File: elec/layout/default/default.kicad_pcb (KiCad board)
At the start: 4 copper layers, 76 x 146 mm, 103 parts, among them J1 ?, J2 ?, Q1 ?, SW1 ?, SW10 ?, SW11 ?, SW12 ?, SW13 ?, SW14 ?, SW15 ?, SW16 ?, SW17 ?, SW18 ?, SW19 ?, SW2 ?, SW20 ?, SW21 ?, SW22 ?, SW23 ?, SW24 ?, SW25 ?, SW26 ?, SW27 ?, SW28 ?, SW29 ?, SW3 ?, SW30 ?, SW31 ?, SW32 ?, SW33 ?, SW34 ?, SW35 ?, SW36 ?, SW37 ?, SW38 ?, SW39 ?, SW4 ?, SW40 ?, SW5 ?, SW6 ?, SW7 ?, SW8 ?, SW9 ?, U1 ?, U2 ?, U3 ?, U4 ?, U5 ?, U6 ?, U7 ?, U8 ?

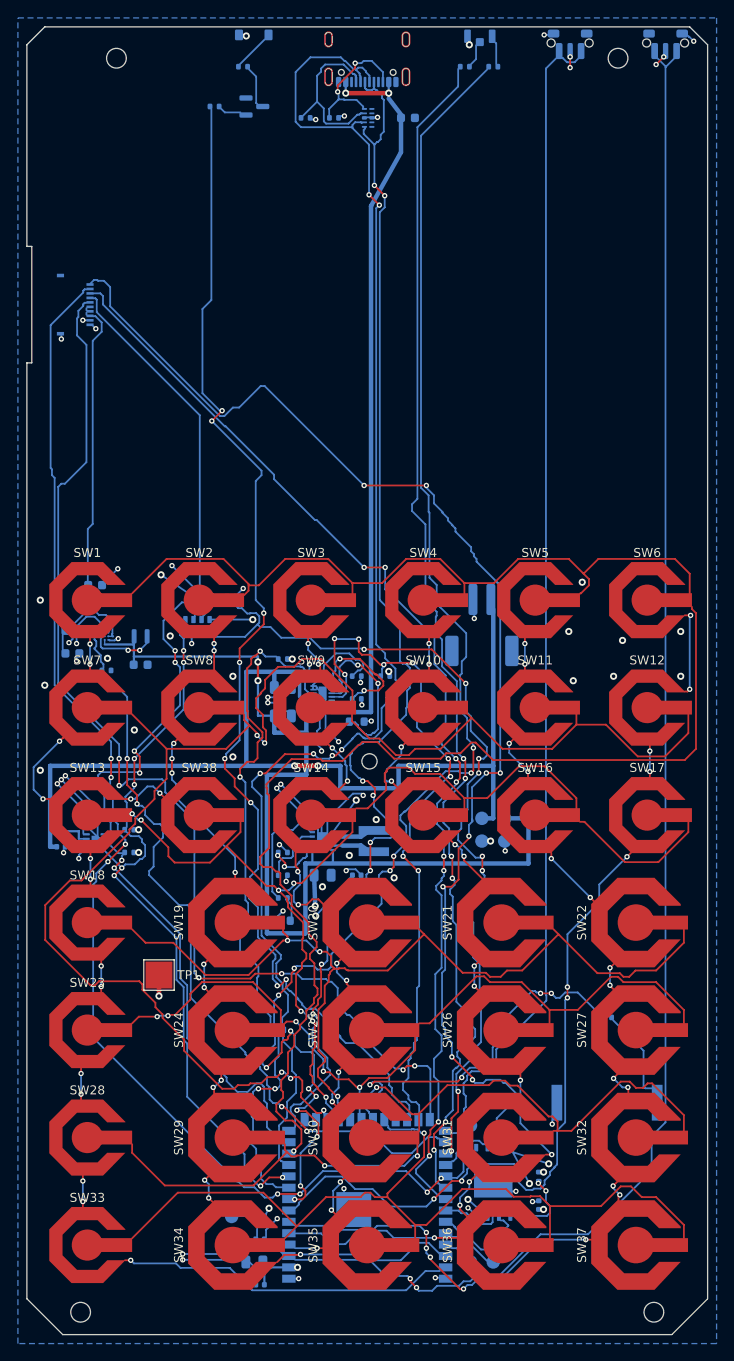
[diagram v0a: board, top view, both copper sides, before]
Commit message: mip: vendor 3D models; RV-8263 and FH34SRJ land fixes; full reroute
Barnaby's vendor STEP for U6 (TPS61099YFFT), U7 (RV-8263-C7), U8 (Micron
MT29F2G01) and J2 (Hirose FH34SRJ-10S) replace the stand-ins. Landing them
caught two footprint faults:

- RV-8263-C7: the land had been copied from the datasheet's bottom view,
  so it was mirrored. Fixed in the generator, library and board (U7).
- FH34SRJ: the catalogue's 3.3 mm is the mounting pattern's overall
  height, not centre to centre, so the fitting lands were 0.8 mm too far
  out (now 2.5). The mouth is 3.025 from the pad row, not 3.70, so J2
  moves to X 6.375 to keep the mouth at X 3.35 and the tail's slack.

The YFF0006 clearance override is now in the generator. route_signals:
a ground-tail via the grid squeezes in with no room to nudge is replaced
by a track to a neighbouring ground pad (U1 pin 3 beside usb_dm).
Stripped and fully rerouted: audit, check_ends, check_pour clean.

Co-Authored-By: Claude Opus 5.5 (1M context) <noreply@anthropic.com>
Claude-Session: https://claude.ai/code/session_01Fsrot3PauY1JdFC7HgzJ33
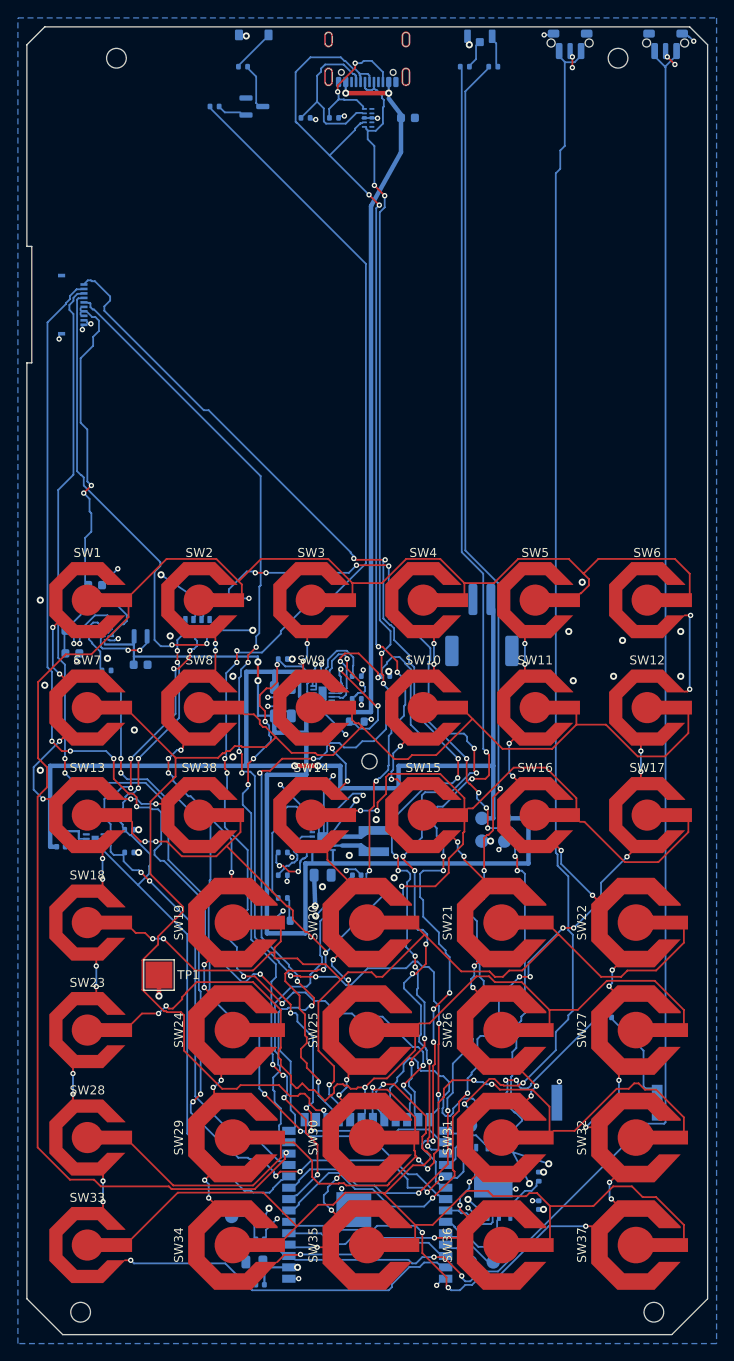
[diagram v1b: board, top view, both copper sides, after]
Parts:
- moved J2 0.67 mm to (6.38, 31.0)
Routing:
- net gnd: track 125.6 -> 74.9 mm, vias 72 -> 62
- net row0: track 200.1 -> 180.1 mm
- net chg_stat2: track 92.8 -> 74.6 mm, vias 10 -> 8
- net row1: track 164.0 -> 146.3 mm, vias 5 -> 1
- net ir_led: track 132.2 -> 149.3 mm
- net row2: track 117.7 -> 133.7 mm, vias 7 -> 8
- net mip_sck: track 145.0 -> 132.8 mm
- net i2c_scl: track 86.2 -> 76.1 mm
- net extcomin: track 41.1 -> 50.2 mm, vias 0 -> 2
- net row6: track 95.3 -> 104.3 mm
- net row5: track 91.4 -> 100.0 mm, vias 3 -> 5
- net mip_clkoe: track 97.7 -> 106.0 mm, vias 8 -> 12
- net usb_dm: track 157.1 -> 149.1 mm
- net col5: track 89.8 -> 82.0 mm, vias 9 -> 11
- net col3: track 56.2 -> 48.8 mm
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
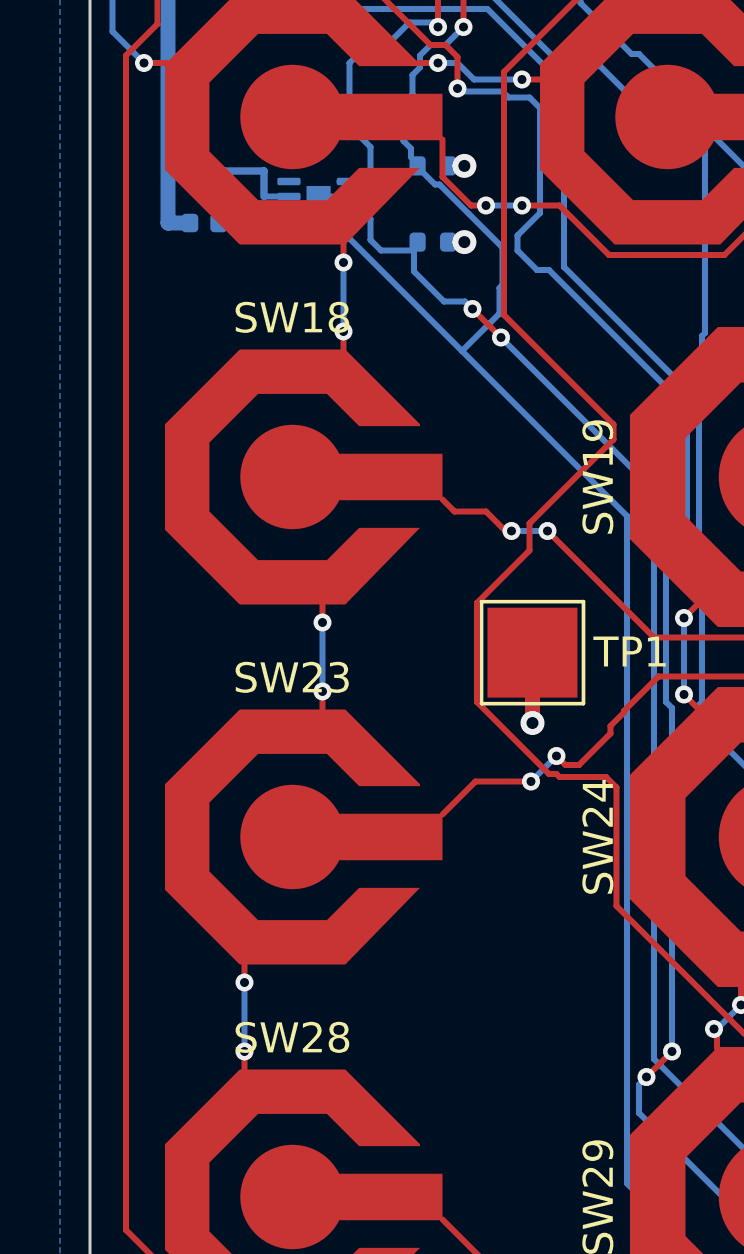
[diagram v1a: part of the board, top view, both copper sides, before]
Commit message: mip: U4 gnd pins 1 and 4 joined to the exposed pad
Barnaby's DRC found U4 pins 1 and 4 unconnected. check_pour counted a pad
as reached when the predicted pour only touched its edge; the pins sit
inside the 0.5 mm clearance of their bat and cell neighbours, so the pour
stopped on their boundary. It now needs real overlap, flags exactly those
two, and route_signals ties each to U4's exposed pad (0.36 mm). check_pour
is now part of route_signals' cache key, since it decides which pads are
stranded. Audit, check_ends, check_pour clean.

Co-Authored-By: Claude Opus 5.5 (1M context) <noreply@anthropic.com>
Claude-Session: https://claude.ai/code/session_01Fsrot3PauY1JdFC7HgzJ33
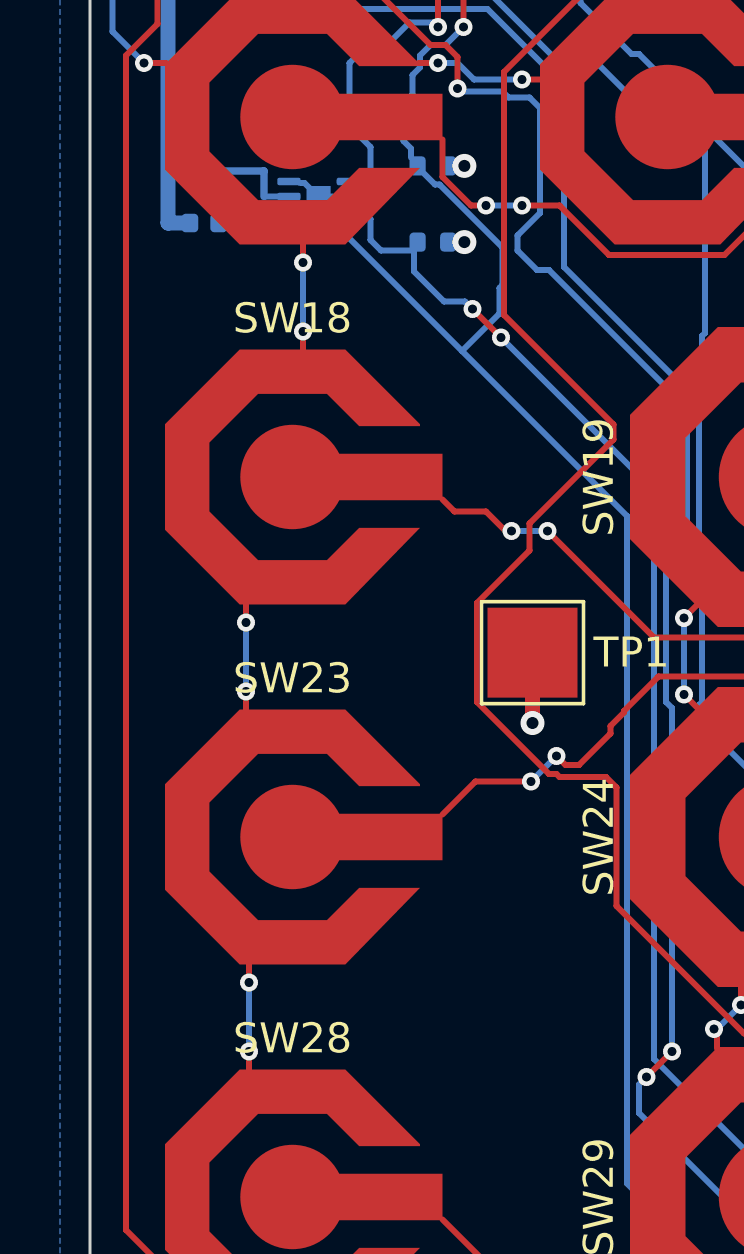
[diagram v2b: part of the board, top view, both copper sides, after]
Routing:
- net gnd: track 74.9 -> 75.6 mm
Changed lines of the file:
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@@
 	)
 	(segment
-		(start 8.45 92.2)
-		(end 8.45 92.85)
+		(start 7.1 92.2)
+		(end 7.1 92.85)
 		(width 0.2)
 		(layer "F.Cu")
@@
 	)
 	(segment
-		(start 8.45 92.85)
-		(end 8.45 95.15)
-		(width 0.2)
-		(layer "B.Cu")
-		(net "col0")
-	)
-	(segment
-		(start 8.45 95.15)
-		(end 8.45 95.8)
+		(start 7.1 92.85)
+		(end 7.1 95.15)
+		(width 0.2)
+		(layer "B.Cu")
+		(net "col0")
+	)
+	(segment
+		(start 7.1 95.15)
+		(end 7.1 95.8)
 		(width 0.2)
 		(layer "F.Cu")
@@
 	)
 	(segment
-		(start 7.75 104.2)
-		(end 7.75 104.85)
+		(start 5.2 104.2)
+		(end 5.2 104.85)
 		(width 0.2)
 		(layer "F.Cu")
@@
 	)
 	(segment
-		(start 7.75 104.85)
-		(end 7.75 107.15)
-		(width 0.2)
-		(layer "B.Cu")
-		(net "col0")
-	)
-	(segment
-		(start 7.75 107.15)
-		(end 7.75 107.8)
+		(start 5.2 104.85)
+		(end 5.2 107.15)
+		(width 0.2)
+		(layer "B.Cu")
+		(net "col0")
+	)
+	(segment
+		(start 5.2 107.15)
+		(end 5.2 107.8)
 		(width 0.2)
 		(layer "F.Cu")
@@
 	)
 	(segment
-		(start 5.15 116.2)
-		(end 5.15 116.85)
+		(start 5.3 116.2)
+		(end 5.3 116.85)
 		(width 0.2)
 		(layer "F.Cu")
@@
 	)
 	(segment
-		(start 5.15 116.85)
-		(end 5.15 119.15)
-		(width 0.2)
-		(layer "B.Cu")
-		(net "col0")
-	)
-	(segment
-		(start 5.15 119.15)
-		(end 5.15 119.8)
+		(start 5.3 116.85)
+		(end 5.3 119.15)
+		(width 0.2)
+		(layer "B.Cu")
+		(net "col0")
+	)
+	(segment
+		(start 5.3 119.15)
+		(end 5.3 119.8)
 		(width 0.2)
 		(layer "F.Cu")
@@
 	)
 	(segment
+		(start 7 91.6)
+		(end 7.15 91.6)
+		(width 0.2)
+		(layer "B.Cu")
+		(net "gnd")
+	)
+	(segment
+		(start 7.15 91.6)
+		(end 7.3 91.45)
+		(width 0.2)
+		(layer "B.Cu")
+		(net "gnd")
+	)
+	(segment
+		(start 7 90.2)
+		(end 7.15 90.2)
+		(width 0.2)
+		(layer "B.Cu")
+		(net "gnd")
+	)
+	(segment
+		(start 7.15 90.2)
+		(end 7.3 90.35)
+		(width 0.2)
+		(layer "B.Cu")
+		(net "gnd")
+	)
+	(segment
 		(start 8.25 90.65)
 		(end 8 90.65)
@@
 	)
 	(via
-		(at 8.45 92.85)
-		(size 0.6)
-		(drill 0.3)
-		(layers "F.Cu" "B.Cu")
-		(net "col0")
-	)
-	(via
-		(at 8.45 95.15)
-		(size 0.6)
-		(drill 0.3)
-		(layers "F.Cu" "B.Cu")
-		(net "col0")
-	)
-	(via
-		(at 7.75 104.85)
-		(size 0.6)
-		(drill 0.3)
-		(layers "F.Cu" "B.Cu")
-		(net "col0")
-	)
-	(via
-		(at 7.75 107.15)
-		(size 0.6)
-		(drill 0.3)
-		(layers "F.Cu" "B.Cu")
-		(net "col0")
-	)
-	(via
-		(at 5.15 116.85)
-		(size 0.6)
-		(drill 0.3)
-		(layers "F.Cu" "B.Cu")
-		(net "col0")
-	)
-	(via
-		(at 5.15 119.15)
-		(size 0.6)
-		(drill 0.3)
+		(at 7.1 92.85)
+		(size 0.6)
+		(drill 0.3)
+		(layers "F.Cu" "B.Cu")
+		(net "col0")
+	)
+	(via
+		(at 7.1 95.15)
+		(size 0.6)
+		(drill 0.3)
+		(layers "F.Cu" "B.Cu")
+		(net "col0")
+	)
+	(via
+		(at 5.2 104.85)
+		(size 0.6)
+		(drill 0.3)
+		(layers "F.Cu" "B.Cu")
+		(net "col0")
+	)
+	(via
+		(at 5.2 107.15)
+		(size 0.6)
+		(drill 0.3)
+		(layers "F.Cu" "B.Cu")
+		(net "col0")
+	)
+	(via
+		(at 5.3 116.85)
+		(size 0.6)
+		(drill 0.3)
+		(layers "F.Cu" "B.Cu")
+		(net "col0")
+	)
+	(via
+		(at 5.3 119.15)
+		(size 0.6)
+		(drill 0.3)

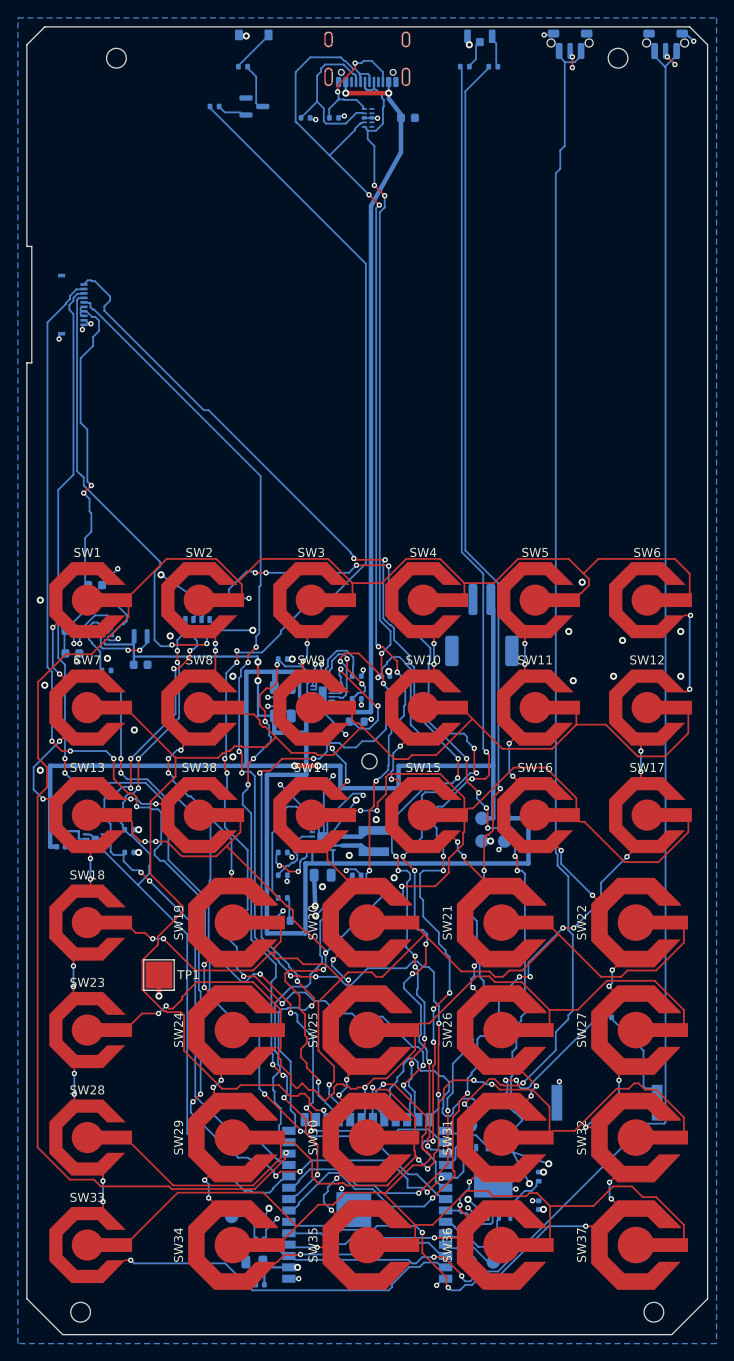
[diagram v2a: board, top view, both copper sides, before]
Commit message: ls027: 2.7in LS027 board placed, IMU+mag, front light switch, power routed
Co-Authored-By: Claude Opus 5.5 (1M context) <noreply@anthropic.com>
Claude-Session: https://claude.ai/code/session_01Fsrot3PauY1JdFC7HgzJ33
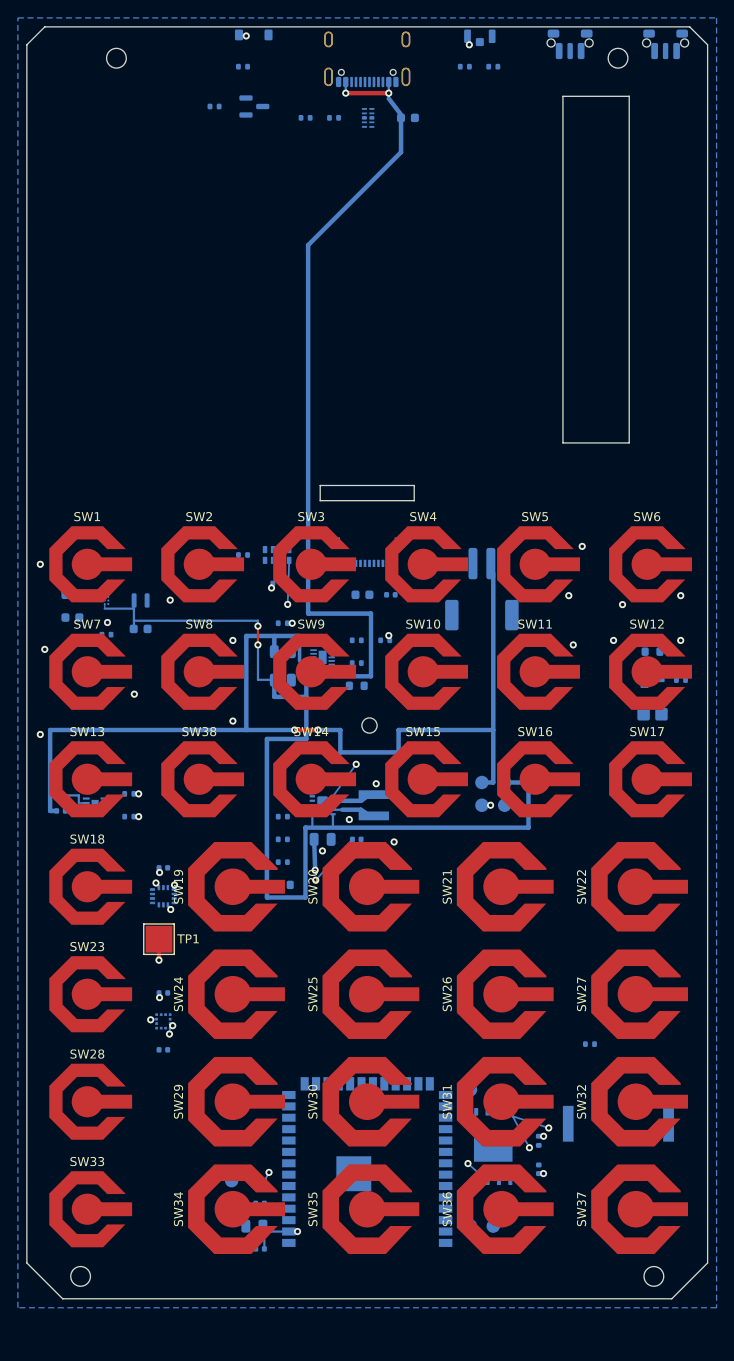
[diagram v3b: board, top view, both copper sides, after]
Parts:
- added C16: ?, Capacitor_SMD:C_0402_1005Metric, B.Cu at (15.2, 93.9)
- added C17: ?, Capacitor_SMD:C_0402_1005Metric, B.Cu at (15.2, 107.9)
- added C18: ?, Capacitor_SMD:C_0402_1005Metric, B.Cu at (15.2, 114.2)
- added C19: ?, Capacitor_SMD:C_0402_1005Metric, B.Cu at (40.6, 63.4)
- added J3: ?, hp42s:Azumo_FLP_LED_WirePads, B.Cu at (69.8, 76.7)
- added Q2: ?, Package_TO_SOT_SMD:SOT-323_SC-70, B.Cu at (69.8, 72.9)
- added R23: ?, Resistor_SMD:R_0603_1608Metric, B.Cu at (69.8, 69.8)
- added R24: ?, Resistor_SMD:R_0402_1005Metric, B.Cu at (73.0, 72.9)
- added U10: ?, hp42s:ST_LGA-12_2x2mm_P0.5mm, B.Cu at (15.2, 111.0)
- added U9: ?, hp42s:ST_LGA-14L_3x2.5mm_P0.5mm, B.Cu at (15.2, 97.1)
- moved J2 42.8 mm to (38.0, 59.9), turned to 0 degrees
- moved C10 29.9 mm to (37.5, 63.4)
- moved U7 11.8 mm to (27.9, 59.0)
- moved C14 9.01 mm to (27.9, 62.1)
- moved R15 4.81 mm to (24.1, 59.0)
- moved R16 4.00 mm to (57.1, 124.4)
- moved C11 4.00 mm to (12.7, 67.2)
- moved C12 4.00 mm to (5.08, 63.4)
- moved C13 4.00 mm to (5.08, 65.9)
- moved C2 4.00 mm to (28.6, 69.8)
- moved C3 4.00 mm to (28.6, 72.9)
- moved C4 4.00 mm to (33.0, 90.7)
- moved C5 4.00 mm to (36.8, 90.7)
- moved C6 4.00 mm to (3.81, 87.5)
- moved C7 4.00 mm to (26.0, 131.3)
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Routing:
- net row0: track 180.1 -> 0.00 mm, vias 1 -> 0
- net en: track 178.0 -> 0.00 mm, vias 2 -> 0
- net led_red: track 149.7 -> 0.00 mm, vias 4 -> 0
- net ir_led: track 149.3 -> 0.00 mm, vias 8 -> 0
- net usb_dm: track 149.1 -> 0.00 mm, vias 6 -> 0
- net row1: track 146.3 -> 0.00 mm, vias 1 -> 0
- net mip_mosi: track 145.4 -> 0.00 mm, vias 10 -> 0
- net usb_dp: track 140.8 -> 0.00 mm, vias 8 -> 0
- net led_green: track 136.6 -> 0.00 mm, vias 8 -> 0
- net row2: track 133.7 -> 0.00 mm, vias 8 -> 0
- net mip_sck: track 132.8 -> 0.00 mm, vias 8 -> 0
- net boot: track 131.7 -> 0.00 mm, vias 2 -> 0
- net mip_cs: track 130.9 -> 0.00 mm, vias 4 -> 0
- net mip_disp: track 121.8 -> 0.00 mm, vias 8 -> 0
- net mip_clkoe: track 106.0 -> 0.00 mm, vias 12 -> 0
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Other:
- board size 76 x 146 mm -> 76 x 142 mm
